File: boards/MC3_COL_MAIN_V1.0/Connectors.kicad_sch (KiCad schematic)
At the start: 10 parts, among them J3 ENC_leaf1, J4 ENC_leaf2, J5 ENC_leaf3, J6 ENC_leaf4

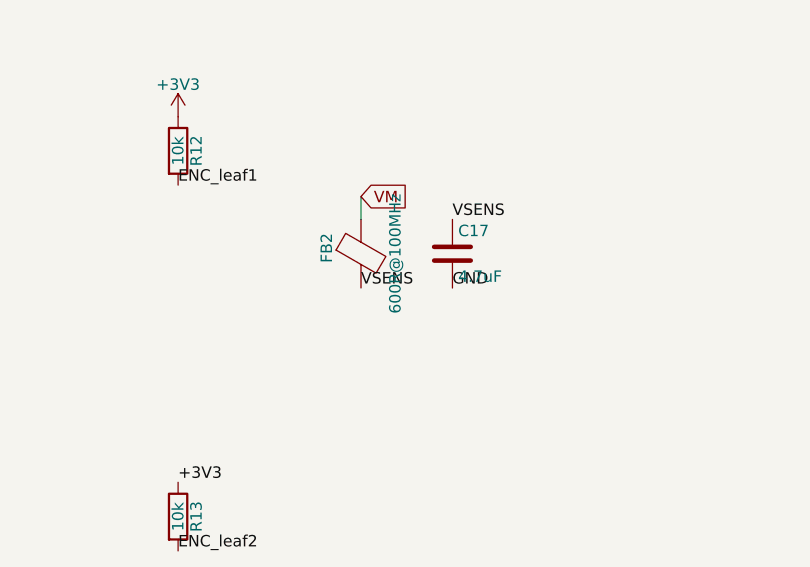
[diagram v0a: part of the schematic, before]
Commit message: Yaw encoder: AEDR-8300 (U9, C22453800) on TIM2 PA15/PB3; SWO dropped for RTT; debug UART PC10/PC11 (J2 old SWO pin = DBG_TX, TP8 = DBG_RX); VSENS promoted to global net
Co-Authored-By: Claude Fable 5 <noreply@anthropic.com>
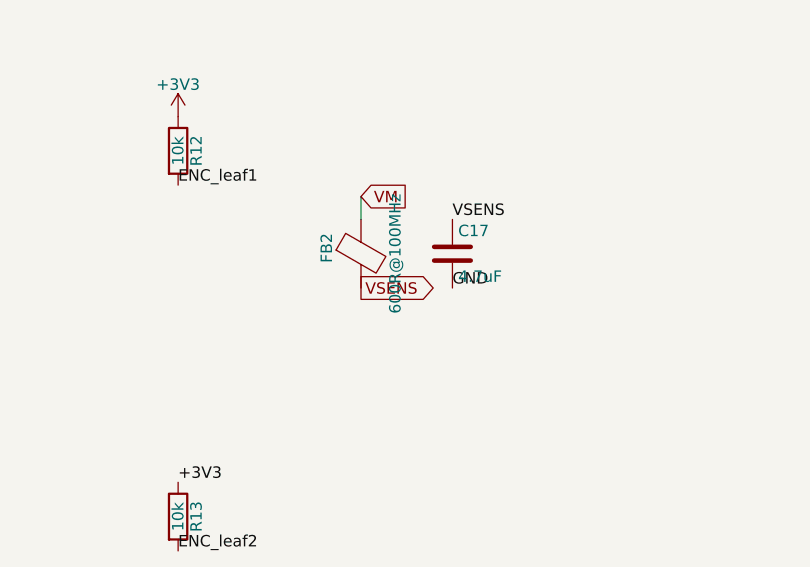
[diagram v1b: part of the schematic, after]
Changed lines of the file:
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@@
 	(generator_version "10.0")
 	(paper "A4")
-	(text "Review 2026-08-22: FFC VIN now from VSENS = VM filtered by FB61 + C63."
-		(exclude_from_sim no)
-		(at 30 195 0)
-		(effects
-			(font
-				(size 1.5 1.5)
-			)
-		)
-	)
-	(text "Encoder interface - four 0.5 mm FFCs, one per leaf, to the LX34311 sensor boards (COL-COTS-0016). Contract: VIN 4-6 V from VM, GND, SIG open-drain pulled to +3V3 here (10k), spare unassigned. Vault: Main-Board-01 Encoder Interface / Connectors. Motor pads are on the MotorChannel sheet; supply pads on Power."
-		(exclude_from_sim no)
-		(at 30 25 0)
-		(effects
-			(font
-				(size 1.5 1.5)
-			)
-		)
-	)
 	(no_connect
 		(at 54.61 134.62)
@@
 	(wire
 		(pts
-			(xy 54.61 49.53) (xy 44.45 49.53)
+			(xy 54.61 49.53)
+			(xy 44.45 49.53)
 		)
 		(stroke
@@
 	(wire
 		(pts
-			(xy 54.61 127) (xy 52.07 127)
+			(xy 54.61 127)
+			(xy 52.07 127)
 		)
 		(stroke
@@
 	(wire
 		(pts
-			(xy 54.61 52.07) (xy 52.07 52.07)
+			(xy 54.61 52.07)
+			(xy 52.07 52.07)
 		)
 		(stroke
@@
 	(wire
 		(pts
-			(xy 54.61 87.63) (xy 52.07 87.63)
+			(xy 54.61 87.63)
+			(xy 52.07 87.63)
 		)
 		(stroke
@@
 	(wire
 		(pts
-			(xy 120.65 52.07) (xy 120.65 49.53)
+			(xy 120.65 52.07)
+			(xy 120.65 49.53)
 		)
 		(stroke
@@
 	(wire
 		(pts
-			(xy 54.61 167.64) (xy 52.07 167.64)
+			(xy 54.61 167.64)
+			(xy 52.07 167.64)
 		)
 		(stroke
@@
 	(wire
 		(pts
-			(xy 54.61 132.08) (xy 52.07 132.08)
+			(xy 54.61 132.08)
+			(xy 52.07 132.08)
 		)
 		(stroke
@@
 	(wire
 		(pts
-			(xy 54.61 92.71) (xy 52.07 92.71)
+			(xy 54.61 92.71)
+			(xy 52.07 92.71)
 		)
 		(stroke
@@
 	(wire
 		(pts
-			(xy 54.61 172.72) (xy 52.07 172.72)
+			(xy 54.61 172.72)
+			(xy 52.07 172.72)
 		)
 		(stroke
@@
 	(wire
 		(pts
-			(xy 54.61 46.99) (xy 52.07 46.99)
+			(xy 54.61 46.99)
+			(xy 52.07 46.99)
 		)
 		(stroke
@@
 		)
 	)
+	(text "Review 2026-08-22: FFC VIN now from VSENS = VM filtered by FB61 + C63."
+		(at 30 195 0)
+		(effects
+			(font
+				(size 1.5 1.5)
+			)
+		)
+	)
+	(text "Encoder interface - four 0.5 mm FFCs, one per leaf, to the LX34311 sensor boards (COL-COTS-0016). Contract: VIN 4-6 V from VM, GND, SIG open-drain pulled to +3V3 here (10k), spare unassigned. Vault: Main-Board-01 Encoder Interface / Connectors. Motor pads are on the MotorChannel sheet; supply pads on Power."
+		(at 30 25 0)
+		(effects
+			(font
+				(size 1.5 1.5)
+			)
+		)
+	)
 	(label "GND"
 		(at 54.61 90.17 180)
@@
 	(label "ENC_leaf2"
 		(at 100.33 88.9 0)
-		(effects
-			(font
-				(size 1.27 1.27)
-			)
-			(justify left bottom)
-		)
-	)
-	(label "VSENS"
-		(at 120.65 59.69 0)
 		(effects
 			(font
@@
 				)
 			)
+		)
+	)
+	(global_label "VSENS"
+		(shape output)
+		(at 120.65 59.69 0)
+		(effects
+			(font
+				(size 1.27 1.27)
+			)
+			(justify left)
 		)
 	)
@@
 		(at 59.69 49.53 0)
 		(unit 1)
-		(body_style 1)
 		(exclude_from_sim no)
 		(in_bom yes)
 		(on_board yes)
-		(in_pos_files yes)
 		(dnp no)
 		(property "Reference" "J3"
@@
 			)
 		)
+		(body_style 1)
+		(in_pos_files yes)
 		(pin "2"
 		)
@@
 		(at 44.45 49.53 90)
 		(unit 1)
-		(body_style 1)
 		(exclude_from_sim no)
 		(in_bom yes)
 		(on_board yes)
-		(in_pos_files yes)
 		(dnp no)
 		(property "Reference" "#PWR09"
@@
 			)
 		)
+		(body_style 1)
+		(in_pos_files yes)
 		(pin "1"
 		)
@@
 		(at 59.69 170.18 0)
 		(unit 1)
-		(body_style 1)
 		(exclude_from_sim no)
 		(in_bom yes)
 		(on_board yes)
-		(in_pos_files yes)
 		(dnp no)
 		(property "Reference" "J6"
@@
 			)
 		)
+		(body_style 1)
+		(in_pos_files yes)
 		(pin "2"
 		)
@@
 		(at 100.33 40.64 0)
 		(unit 1)
-		(body_style 1)
 		(exclude_from_sim no)
 		(in_bom yes)
 		(on_board yes)
-		(in_pos_files yes)
 		(dnp no)
 		(property "Reference" "#PWR010"
@@
 			)
 		)
+		(body_style 1)
+		(in_pos_files yes)
 		(pin "1"
 		)
@@
 		(at 100.33 85.09 0)
 		(unit 1)
-		(body_style 1)
 		(exclude_from_sim no)
 		(in_bom yes)
 		(on_board yes)
-		(in_pos_files yes)
 		(dnp no)
 		(property "Reference" "R13"
@@
 			)
 		)
+		(body_style 1)
+		(in_pos_files yes)
 		(pin "1"
 		)
@@
 		(at 100.33 165.1 0)
 		(unit 1)
-		(body_style 1)
 		(exclude_from_sim no)
 		(in_bom yes)
 		(on_board yes)
-		(in_pos_files yes)
 		(dnp no)
 		(property "Reference" "R15"
@@
 			)
 		)
+		(body_style 1)
+		(in_pos_files yes)
 		(pin "1"
 		)
@@
 		(at 130.81 55.88 0)
 		(unit 1)
-		(body_style 1)
 		(exclude_from_sim no)
 		(in_bom yes)
 		(on_board yes)
-		(in_pos_files yes)
 		(dnp no)
 		(property "Reference" "C17"
@@
 			)
 		)
+		(body_style 1)
+		(in_pos_files yes)
 		(pin "1"
 		)
@@
 		(at 59.69 90.17 0)
 		(unit 1)
-		(body_style 1)
 		(exclude_from_sim no)
 		(in_bom yes)
 		(on_board yes)
-		(in_pos_files yes)
 		(dnp no)
 		(property "Reference" "J4"
@@
 			)
 		)
+		(body_style 1)
+		(in_pos_files yes)
 		(pin "3"
 		)
@@
 		(at 59.69 129.54 0)
 		(unit 1)
-		(body_style 1)
 		(exclude_from_sim no)
 		(in_bom yes)
 		(on_board yes)
-		(in_pos_files yes)
 		(dnp no)
 		(property "Reference" "J5"
@@
 			)
 		)
+		(body_style 1)
+		(in_pos_files yes)
 		(pin "4"
 		)
@@
 		(at 120.65 55.88 0)
 		(unit 1)
-		(body_style 1)
 		(exclude_from_sim no)
 		(in_bom yes)
 		(on_board yes)
-		(in_pos_files yes)
 		(dnp no)
 		(property "Reference" "FB2"
@@
 			)
 		)
+		(body_style 1)
+		(in_pos_files yes)
 		(pin "2"
 		)
@@
 		(at 100.33 44.45 0)
 		(unit 1)
-		(body_style 1)
 		(exclude_from_sim no)
 		(in_bom yes)
 		(on_board yes)
-		(in_pos_files yes)
 		(dnp no)
 		(property "Reference" "R12"
@@
 			)
 		)
+		(body_style 1)
+		(in_pos_files yes)
 		(pin "1"
 		)
@@
 		(at 100.33 124.46 0)
 		(unit 1)
-		(body_style 1)
 		(exclude_from_sim no)
 		(in_bom yes)
 		(on_board yes)
-		(in_pos_files yes)
 		(dnp no)
 		(property "Reference" "R14"
@@
 			)
 		)
+		(body_style 1)
+		(in_pos_files yes)
 		(pin "1"
 		)
